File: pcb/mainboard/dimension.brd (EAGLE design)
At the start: 96 x 58 mm, 0 parts

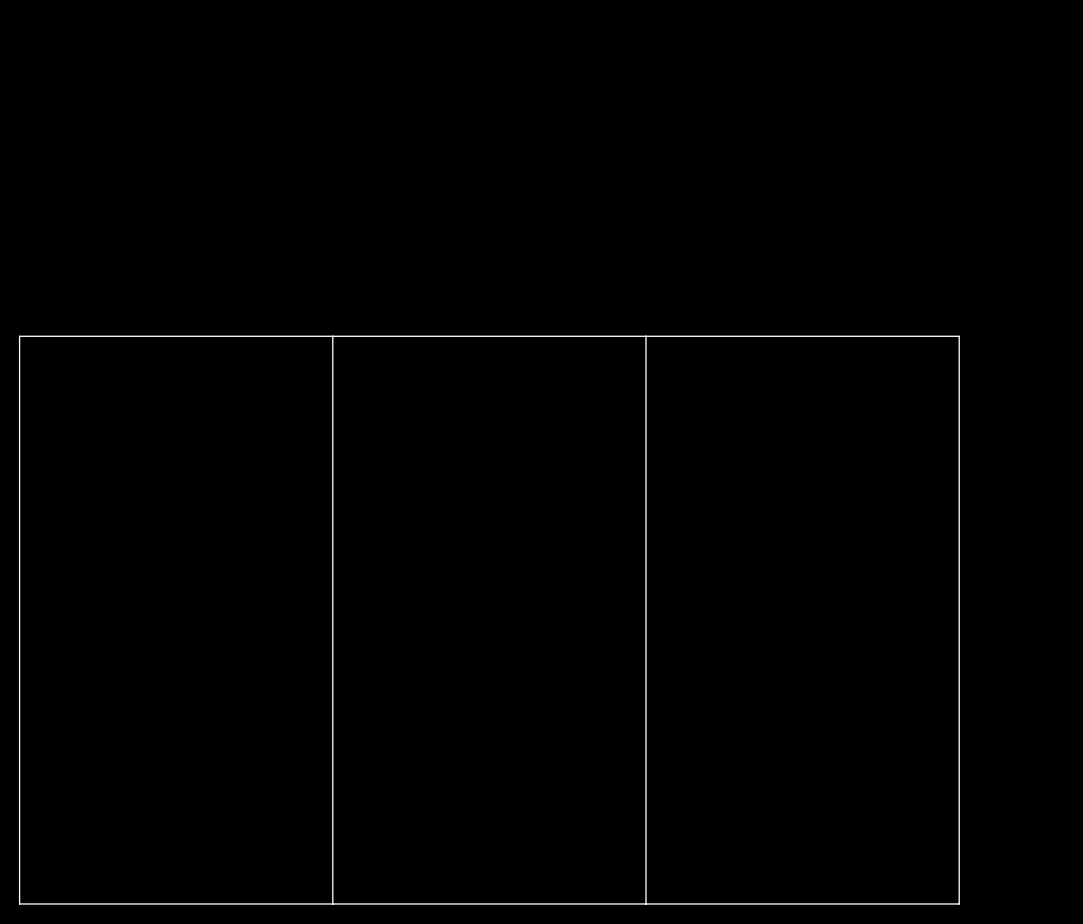
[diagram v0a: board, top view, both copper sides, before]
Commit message: improve panelizing
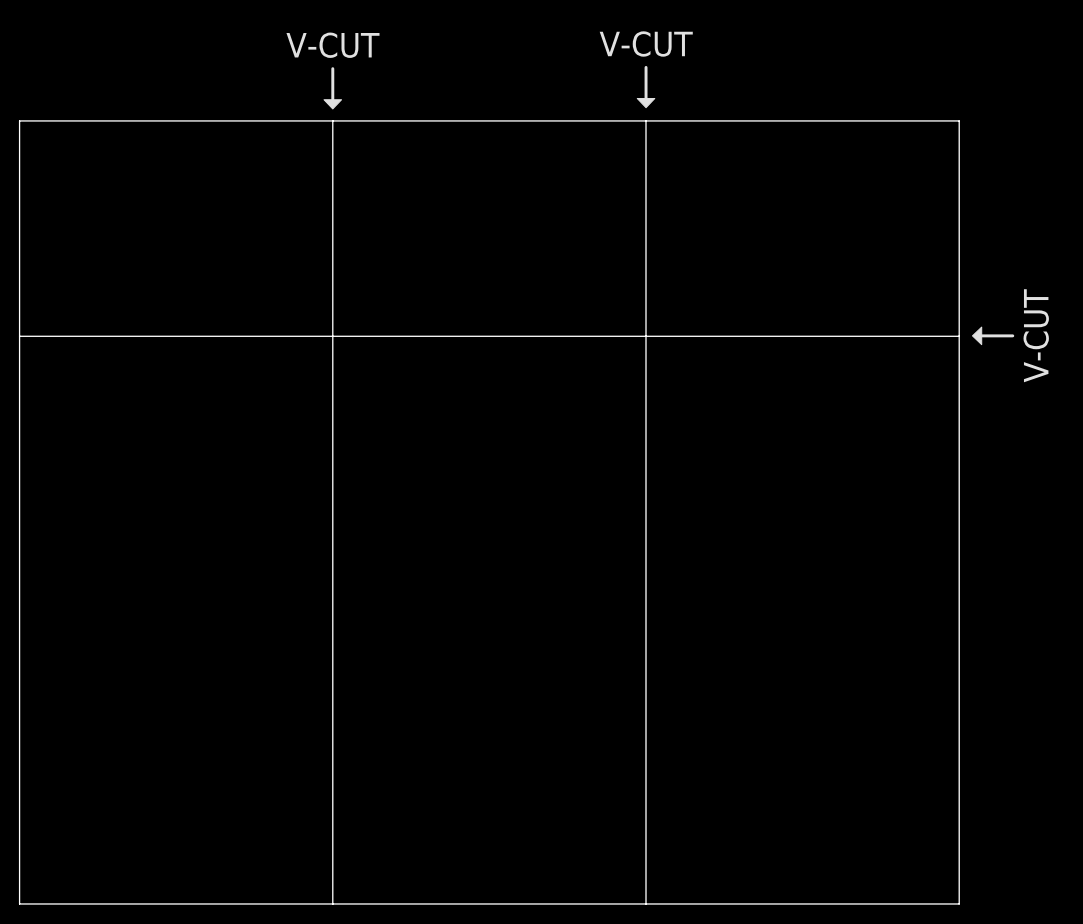
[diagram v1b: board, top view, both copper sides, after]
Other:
- board size 96 x 58 mm -> 96 x 80 mm
- board text added: "V-CUT"
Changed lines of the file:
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@@
 <layer number="48" name="Document" color="7" fill="1" visible="yes" active="yes"/>
 <layer number="49" name="Reference" color="7" fill="1" visible="yes" active="yes"/>
+<layer number="50" name="dxf" color="7" fill="1" visible="no" active="no"/>
 <layer number="51" name="tDocu" color="7" fill="1" visible="yes" active="yes"/>
 <layer number="52" name="bDocu" color="7" fill="1" visible="yes" active="yes"/>
+<layer number="53" name="tGND_GNDA" color="7" fill="9" visible="no" active="no"/>
+<layer number="54" name="bGND_GNDA" color="1" fill="9" visible="no" active="no"/>
+<layer number="56" name="wert" color="7" fill="1" visible="no" active="no"/>
+<layer number="88" name="SimResults" color="9" fill="1" visible="no" active="no"/>
+<layer number="89" name="SimProbes" color="9" fill="1" visible="no" active="no"/>
+<layer number="90" name="Modules" color="5" fill="1" visible="no" active="no"/>
+<layer number="91" name="Nets" color="2" fill="1" visible="no" active="no"/>
+<layer number="92" name="Busses" color="1" fill="1" visible="no" active="no"/>
+<layer number="93" name="Pins" color="2" fill="1" visible="no" active="no"/>
+<layer number="94" name="Symbols" color="4" fill="1" visible="no" active="no"/>
+<layer number="95" name="Names" color="7" fill="1" visible="no" active="no"/>
+<layer number="96" name="Values" color="7" fill="1" visible="no" active="no"/>
+<layer number="97" name="Info" color="7" fill="1" visible="no" active="no"/>
+<layer number="98" name="Guide" color="6" fill="1" visible="no" active="no"/>
+<layer number="100" name="Muster" color="7" fill="1" visible="no" active="no"/>
+<layer number="101" name="Patch_Top" color="12" fill="4" visible="no" active="yes"/>
+<layer number="102" name="Vscore" color="7" fill="1" visible="no" active="yes"/>
+<layer number="103" name="tMap" color="7" fill="1" visible="no" active="yes"/>
+<layer number="104" name="Name" color="16" fill="1" visible="no" active="yes"/>
+<layer number="105" name="tPlate" color="7" fill="1" visible="no" active="yes"/>
+<layer number="106" name="bPlate" color="7" fill="1" visible="no" active="yes"/>
+<layer number="107" name="Crop" color="7" fill="1" visible="no" active="yes"/>
+<layer number="108" name="fp8" color="7" fill="1" visible="no" active="yes"/>
+<layer number="109" name="fp9" color="7" fill="1" visible="no" active="yes"/>
+<layer number="110" name="fp0" color="7" fill="1" visible="no" active="yes"/>
+<layer number="111" name="LPC17xx" color="7" fill="1" visible="yes" active="yes"/>
+<layer number="116" name="Patch_BOT" color="9" fill="4" visible="no" active="yes"/>
+<layer number="121" name="_tsilk" color="7" fill="1" visible="no" active="yes"/>
+<layer number="122" name="_bsilk" color="7" fill="1" visible="no" active="yes"/>
+<layer number="123" name="tTestmark" color="7" fill="1" visible="no" active="yes"/>
+<layer number="124" name="bTestmark" color="7" fill="1" visible="no" active="yes"/>
+<layer number="125" name="_tNames" color="7" fill="1" visible="no" active="yes"/>
+<layer number="131" name="tAdjust" color="7" fill="1" visible="no" active="yes"/>
+<layer number="132" name="bAdjust" color="7" fill="1" visible="no" active="yes"/>
+<layer number="144" name="Drill_legend" color="7" fill="1" visible="no" active="yes"/>
+<layer number="151" name="HeatSink" color="7" fill="1" visible="no" active="yes"/>
+<layer number="199" name="Contour" color="7" fill="1" visible="yes" active="yes"/>
+<layer number="200" name="200bmp" color="1" fill="10" visible="no" active="yes"/>
+<layer number="201" name="201bmp" color="2" fill="10" visible="no" active="yes"/>
+<layer number="202" name="202bmp" color="3" fill="10" visible="no" active="yes"/>
+<layer number="203" name="203bmp" color="4" fill="10" visible="no" active="yes"/>
+<layer number="204" name="204bmp" color="5" fill="10" visible="no" active="yes"/>
+<layer number="205" name="205bmp" color="6" fill="10" visible="no" active="yes"/>
+<layer number="206" name="206bmp" color="7" fill="10" visible="no" active="yes"/>
+<layer number="207" name="207bmp" color="8" fill="10" visible="no" active="yes"/>
+<layer number="208" name="208bmp" color="9" fill="10" visible="no" active="yes"/>
+<layer number="209" name="209bmp" color="7" fill="1" visible="no" active="yes"/>
+<layer number="210" name="210bmp" color="7" fill="1" visible="no" active="yes"/>
+<layer number="211" name="211bmp" color="7" fill="1" visible="no" active="yes"/>
+<layer number="212" name="212bmp" color="7" fill="1" visible="no" active="yes"/>
+<layer number="213" name="213bmp" color="7" fill="1" visible="no" active="yes"/>
+<layer number="214" name="214bmp" color="7" fill="1" visible="no" active="yes"/>
+<layer number="215" name="215bmp" color="7" fill="1" visible="no" active="yes"/>
+<layer number="216" name="216bmp" color="7" fill="1" visible="no" active="yes"/>
+<layer number="217" name="217bmp" color="18" fill="1" visible="no" active="no"/>
+<layer number="218" name="218bmp" color="19" fill="1" visible="no" active="no"/>
+<layer number="219" name="219bmp" color="20" fill="1" visible="no" active="no"/>
+<layer number="220" name="220bmp" color="21" fill="1" visible="no" active="no"/>
+<layer number="221" name="221bmp" color="22" fill="1" visible="no" active="no"/>
+<layer number="222" name="222bmp" color="23" fill="1" visible="no" active="no"/>
+<layer number="223" name="223bmp" color="24" fill="1" visible="no" active="no"/>
+<layer number="224" name="224bmp" color="25" fill="1" visible="no" active="no"/>
+<layer number="250" name="Descript" color="3" fill="1" visible="no" active="no"/>
+<layer number="251" name="SMDround" color="12" fill="11" visible="no" active="no"/>
+<layer number="254" name="cooling" color="7" fill="1" visible="no" active="yes"/>
 </layers>
 <board>
 <plain>
+<polygon width="0.1" layer="21">
+<vertex x="32" y="81.225"/>
+<vertex x="32.9" y="82.169"/>
+<vertex x="31.1" y="82.169"/>
+</polygon>
+<wire x1="32" y1="85.344" x2="32" y2="81.788" width="0.3" layer="21"/>
+<text x="32.004" y="86.487" size="2.5" layer="21" font="vector" align="bottom-center">V-CUT</text>
+<polygon width="0.1" layer="21">
+<vertex x="64.004" y="81.352"/>
+<vertex x="64.904" y="82.296"/>
+<vertex x="63.104" y="82.296"/>
+</polygon>
+<wire x1="64.004" y1="85.471" x2="64.004" y2="81.915" width="0.3" layer="21"/>
+<text x="64.008" y="86.614" size="2.5" layer="21" font="vector" align="bottom-center">V-CUT</text>
+<polygon width="0.1" layer="21">
+<vertex x="97.354" y="58.043"/>
+<vertex x="98.298" y="57.143"/>
+<vertex x="98.298" y="58.943"/>
+</polygon>
+<wire x1="101.473" y1="58.043" x2="97.917" y2="58.043" width="0.3" layer="21"/>
+<text x="102.616" y="58.039" size="2.5" layer="21" font="vector" rot="R270" align="bottom-center">V-CUT</text>
 <wire x1="0" y1="0" x2="0" y2="58" width="0" layer="20"/>
-<wire x1="0" y1="58" x2="32" y2="58" width="0" layer="20"/>
-<wire x1="32" y1="58" x2="64" y2="58" width="0" layer="20"/>
-<wire x1="64" y1="58" x2="96" y2="58" width="0" layer="20"/>
+<wire x1="0" y1="58" x2="0" y2="80" width="0" layer="20"/>
+<wire x1="0" y1="80" x2="32" y2="80" width="0" layer="20"/>
+<wire x1="32" y1="80" x2="64" y2="80" width="0" layer="20"/>
+<wire x1="64" y1="80" x2="96" y2="80" width="0" layer="20"/>
+<wire x1="96" y1="80" x2="96" y2="58" width="0" layer="20"/>
 <wire x1="96" y1="58" x2="96" y2="0" width="0" layer="20"/>
 <wire x1="96" y1="0" x2="64" y2="0" width="0" layer="20"/>
 <wire x1="64" y1="0" x2="32" y2="0" width="0" layer="20"/>
 <wire x1="32" y1="0" x2="0" y2="0" width="0" layer="20"/>
-<wire x1="32" y1="58" x2="32" y2="0" width="0" layer="20"/>
-<wire x1="64" y1="58" x2="64" y2="0" width="0" layer="20"/>
+<wire x1="0" y1="58" x2="96" y2="58" width="0" layer="20"/>
+<wire x1="32" y1="80" x2="32" y2="0" width="0" layer="20"/>
+<wire x1="64" y1="80" x2="64" y2="0" width="0" layer="20"/>
 </plain>
 <attributes>
